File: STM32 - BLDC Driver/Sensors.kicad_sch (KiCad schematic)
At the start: 12 parts, among them U5 BMI088

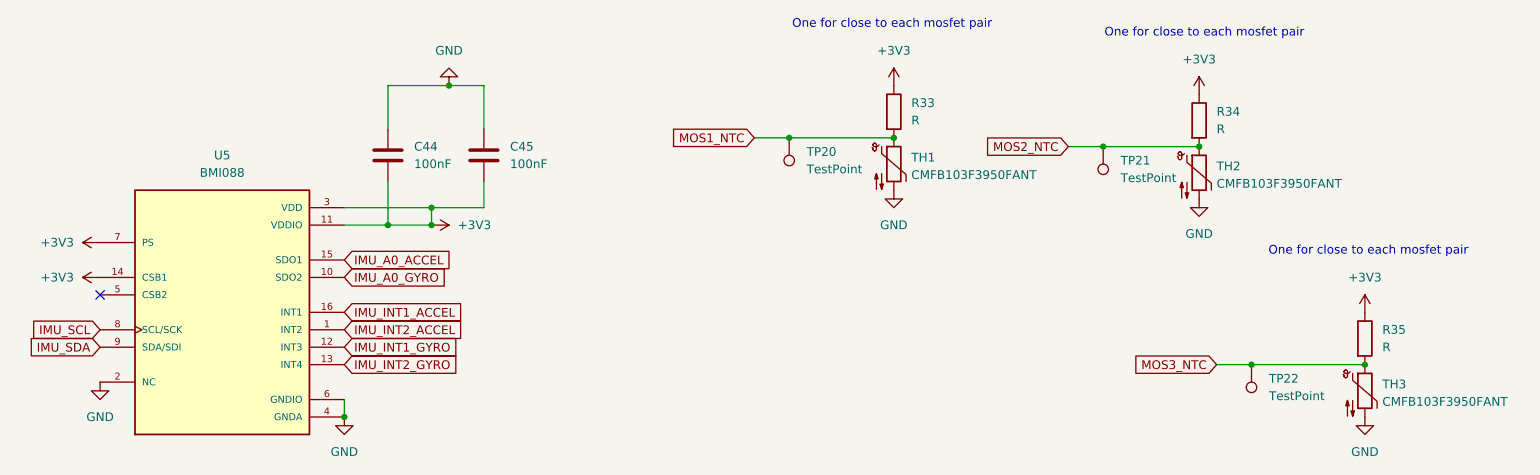
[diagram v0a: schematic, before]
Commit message: Started assigning footprints
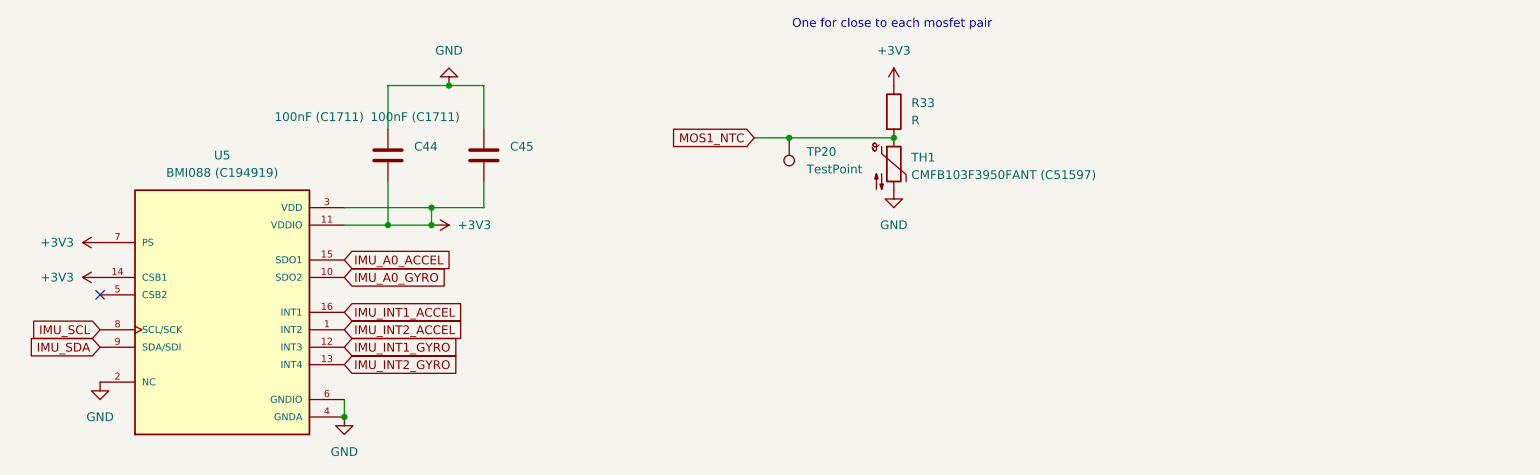
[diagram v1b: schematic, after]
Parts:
- removed R34, R35: R, symbol Device:R
- removed TH2, TH3: CMFB103F3950FANT, symbol Device:Thermistor_NTC
- removed TP21, TP22: TestPoint, symbol Connector:TestPoint
- C44, C45: value 100nF -> 100nF (C1711); footprint (none) -> Capacitor_SMD:C_0805_2012Metric_Pad1.18x1.45mm_HandSolder
- TH1: value CMFB103F3950FANT -> CMFB103F3950FANT (C51597); footprint (none) -> Resistor_SMD:R_0805_2012Metric_Pad1.20x1.40mm_HandSolder
- U5: value BMI088 -> BMI088 (C194919)
